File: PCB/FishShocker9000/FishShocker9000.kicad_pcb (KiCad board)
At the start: 2 copper layers, 160 parts, among them J1 Barrel_Jack, J10 P70-1000045R, J11 P70-1000045R, J12 P70-1000045R, J13 P70-1000045R, J14 P70-1000045R, J15 P70-1000045R, J16 P70-1000045R, J17 P70-1000045R, J18 P70-1000045R, J19 P70-1000045R, J20 P70-1000045R, J21 P70-1000045R, J22 P70-1000045R, J23 P70-1000045R, J24 P70-1000045R, J25 P70-1000045R, J26 P70-1000045R, J27 P70-1000045R, J28 P70-1000045R, J29 P70-1000045R, J3 P70-1000045R, J30 P70-1000045R, J31 P70-1000045R, J32 P70-1000045R, J33 P70-1000045R, J34 P70-1000045R, J35 P70-1000045R, J36 P70-1000045R, J37 P70-1000045R, J38 P70-1000045R, J39 P70-1000045R, J4 P70-1000045R, J40 P70-1000045R, J41 P70-1000045R, J42 P70-1000045R, J43 P70-1000045R, J44 P70-1000045R, J45 P70-1000045R, J46 P70-1000045R, J47 P70-1000045R, J48 P70-1000045R, J49 P70-1000045R, J5 P70-1000045R, J50 P70-1000045R, J51 P70-1000045R, J52 P70-1000045R, J53 P70-1000045R, J54 P70-1000045R, J55 P70-1000045R, J56 P70-1000045R, J57 P70-1000045R, J58 P70-1000045R, J59 P70-1000045R, J6 P70-1000045R, J60 P70-1000045R, J61 P70-1000045R, J62 P70-1000045R, J63 P70-1000045R, J64 P70-1000045R, J65 P70-1000045R, J66 P70-1000045R, J67 P70-1000045R, J68 P70-1000045R, J69 P70-1000045R, J7 P70-1000045R, J70 P70-1000045R, J71 P70-1000045R, J72 P70-1000045R, J73 P70-1000045R, J74 P70-1000045R, J75 Screw_Terminal_01x02, J8 P70-1000045R, J9 P70-1000045R, Q2 FQP27P06, U10 SN754410NE, U11 SN754410NE, U12 SN754410NE, U13 SN754410NE, U14 SN754410NE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

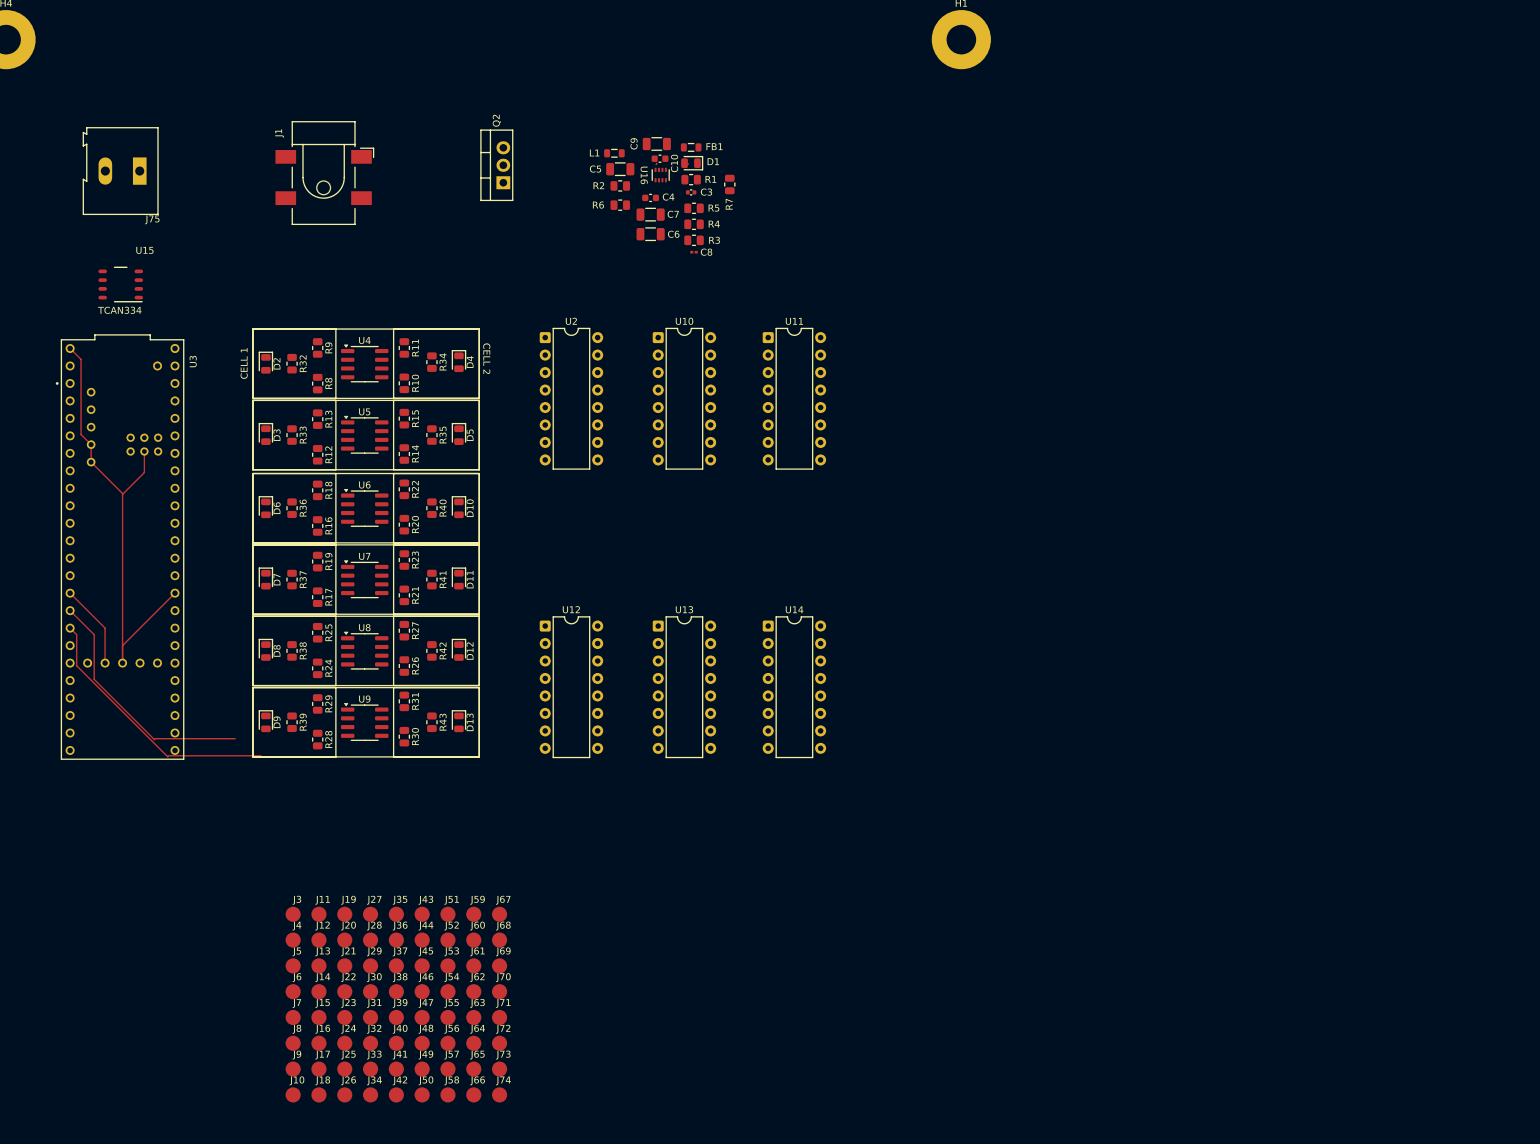
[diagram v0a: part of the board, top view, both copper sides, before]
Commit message: routed PCB except for GND and Pogo Pins
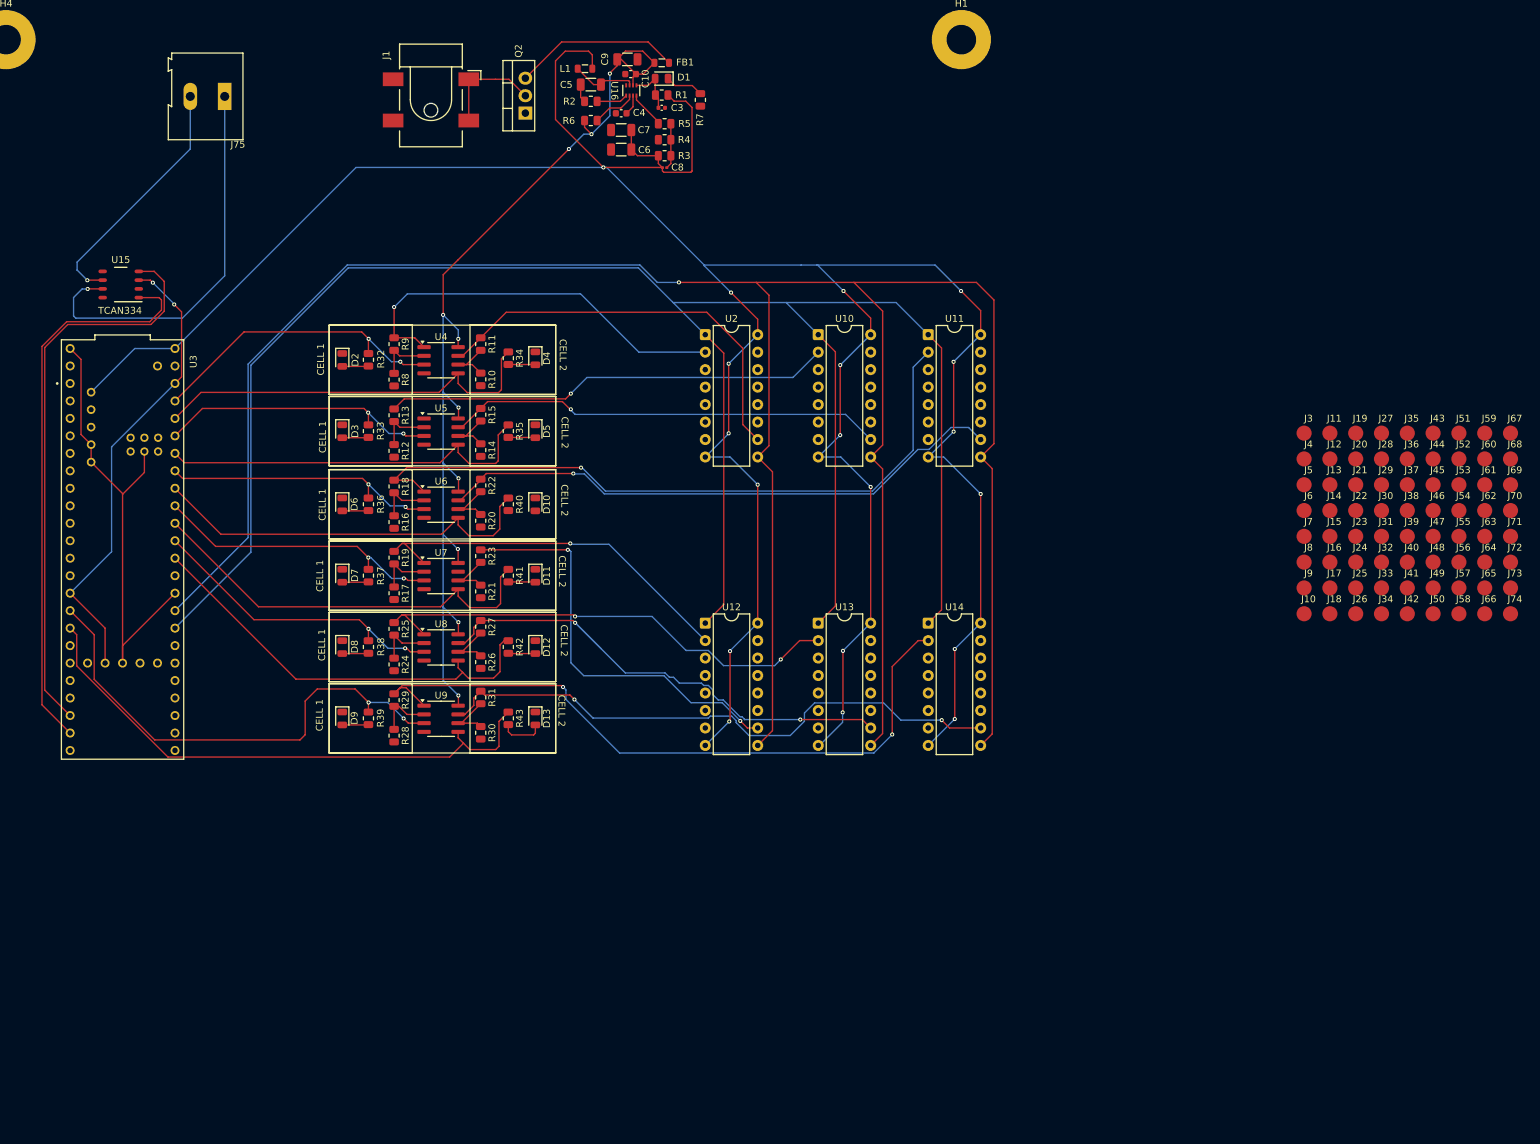
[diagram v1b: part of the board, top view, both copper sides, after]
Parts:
- moved J10 162.7 mm to (205.8, 101.5)
- moved J11 162.7 mm to (209.6, 75.3)
- moved J12 162.7 mm to (209.6, 79.0)
- moved J13 162.7 mm to (209.6, 82.8)
- moved J14 162.7 mm to (209.6, 86.5)
- moved J15 162.7 mm to (209.6, 90.3)
- moved J16 162.7 mm to (209.6, 94.0)
- moved J17 162.7 mm to (209.6, 97.8)
- moved J18 162.7 mm to (209.6, 101.5)
- moved J19 162.7 mm to (213.3, 75.3)
- moved J20 162.7 mm to (213.3, 79.0)
- moved J21 162.7 mm to (213.3, 82.8)
- moved J22 162.7 mm to (213.3, 86.5)
- moved J23 162.7 mm to (213.3, 90.3)
- moved J24 162.7 mm to (213.3, 94.0)
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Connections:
- R32 pad 1: A0 -> A9
- R33 pad 1: A2 -> A7
- R34 pad 1: A1 -> A8
- R35 pad 1: A3 -> A6
- R36 pad 1: A4 -> A5
- R37 pad 1: A6 -> A3
- R38 pad 1: A8 -> A1
- R40 pad 1: A5 -> A4
- R41 pad 1: A7 -> A2
- R42 pad 1: A9 -> A0
- U4 pad 3: A0 -> A9
- U4 pad 5: A1 -> A8
- U5 pad 3: A2 -> A7
- U5 pad 5: A3 -> A6
- U6 pad 3: A4 -> A5
- U6 pad 5: A5 -> A4
- U7 pad 3: A6 -> A3
- U7 pad 5: A7 -> A2
- U8 pad 3: A8 -> A1
- U8 pad 5: A9 -> A0
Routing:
- net BUCK_VOUT: track 0.00 -> 457.6 mm, vias 0 -> 19
- net Polarity Enable 2: track 0.00 -> 365.3 mm, vias 0 -> 1
- net Polarity Enable 1: track 0.00 -> 296.0 mm
- net AMP_RAIL: track 0.00 -> 149.4 mm, vias 0 -> 10
- net CELL11: track 0.00 -> 101.3 mm, vias 0 -> 2
- net CELL5: track 0.00 -> 100.3 mm, vias 0 -> 1
- net CELL12: track 0.00 -> 85.2 mm, vias 0 -> 2
- net CELL6: track 0.00 -> 83.6 mm, vias 0 -> 1
- net RXD: track 0.00 -> 83.2 mm
- net TXD: track 0.00 -> 82.3 mm
- net CELL10: track 0.00 -> 74.1 mm, vias 0 -> 2
- net CELL9: track 0.00 -> 71.1 mm, vias 0 -> 2
- net CELL3: track 0.00 -> 65.1 mm, vias 0 -> 1
- net CELL4: track 0.00 -> 63.8 mm, vias 0 -> 1
- net A0: track 0.00 -> 63.0 mm
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
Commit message: New draft of final PCB layout
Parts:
- added Q1: IRLZ44N, Package_TO_SOT_THT:TO-220-3_Vertical, F.Cu at (123.6, 22.4)
- R7: value 220 -> 330
- moved J10 143.6 mm to (80.2, 171.1)
- moved J11 143.6 mm to (83.9, 144.8)
- moved J12 143.6 mm to (83.9, 148.6)
- moved J13 143.6 mm to (83.9, 152.3)
- moved J14 143.6 mm to (83.9, 156.1)
- moved J15 143.6 mm to (83.9, 159.8)
- moved J16 143.6 mm to (83.9, 163.6)
- moved J17 143.6 mm to (83.9, 167.3)
- moved J18 143.6 mm to (83.9, 171.1)
- moved J19 143.6 mm to (87.7, 144.8)
- moved J20 143.6 mm to (87.7, 148.6)
- moved J21 143.6 mm to (87.7, 152.3)
- moved J22 143.6 mm to (87.7, 156.1)
- moved J23 143.6 mm to (87.7, 159.8)
- moved J24 143.6 mm to (87.7, 163.6)
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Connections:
- net AMP_RAIL renamed BUCK_IN
- D1 pad 2: BUCK_PG -> Net-(D1-A)
- R7 pad 1: GND -> Net-(D1-A)
- R7 pad 2: Net-(D1-K) -> BUCK_VOUT
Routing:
- net GND: track 69.7 -> 138.9 mm, vias 0 -> 4
- net BUCK_PG: track 7.56 -> 21.8 mm, vias 0 -> 1
- net Net-(D1-A): track 0.00 -> 7.48 mm
- net Net-(D10-A): track 0.00 -> 6.54 mm
- net Net-(D1-K): track 5.61 -> 11.7 mm
- net CELL8: track 60.5 -> 65.6 mm
- net CELL3: track 65.1 -> 69.4 mm
- net BUCK_IN: track 149.4 -> 146.0 mm
- net Net-(D12-A): track 3.95 -> 5.37 mm
- net Net-(D4-A): track 3.95 -> 5.33 mm
- net BUCK_VOUT: track 457.6 -> 458.9 mm
- net Net-(D5-A): track 3.95 -> 5.15 mm
- net Net-(D13-A): track 6.46 -> 7.19 mm
- net CELL9: vias 2 -> 1
- added copper zone on F.Cu, net GND
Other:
- board text added: "Barrel Jack"
- board text added: "CAN Bus H/L"
- board text added: "CELL 10"
- board text added: "CELL 11"
- board text added: "CELL 12"
- board text added: "CELL 3"
- board text added: "CELL 4"
- board text added: "CELL 5"
- board text added: "CELL 6"
- board text added: "CELL 7"
- board text added: "CELL 8"
- board text added: "CELL 9"
- board text added: "LED ON = GOOD POWER"
- board text added: "Op-Amps"
- board text added: "Polarity Drivers"
- board text added: "Teensy 4.1"

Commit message: Changed Layout to eb more clean
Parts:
- moved J10 141.4 mm to (194.8, 88.3)
- moved J11 141.4 mm to (198.5, 62.1)
- moved J12 141.4 mm to (198.5, 65.8)
- moved J13 141.4 mm to (198.5, 69.6)
- moved J14 141.4 mm to (198.5, 73.3)
- moved J15 141.4 mm to (198.5, 77.1)
- moved J16 141.4 mm to (198.5, 80.8)
- moved J17 141.4 mm to (198.5, 84.6)
- moved J18 141.4 mm to (198.5, 88.3)
- moved J19 141.4 mm to (202.3, 62.1)
- moved J20 141.4 mm to (202.3, 65.8)
- moved J21 141.4 mm to (202.3, 69.6)
- moved J22 141.4 mm to (202.3, 73.3)
- moved J23 141.4 mm to (202.3, 77.1)
- moved J24 141.4 mm to (202.3, 80.8)
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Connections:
- U10 pad 10: CELL4 -> CELL3
- U10 pad 11: Plate 4.1 -> Plate 3.2
- U10 pad 14: Plate 4.2 -> Plate 3.1
- U10 pad 2: CELL3 -> CELL4
- U10 pad 3: Plate 3.1 -> Plate 4.2
- U10 pad 6: Plate 3.2 -> Plate 4.1
- U11 pad 10: CELL6 -> CELL5
- U11 pad 11: Plate 6.1 -> Plate 5.2
- U11 pad 14: Plate 6.2 -> Plate 5.1
- U11 pad 2: CELL5 -> CELL6
- U11 pad 3: Plate 5.1 -> Plate 6.2
- U11 pad 6: Plate 5.2 -> Plate 6.1
- U12 pad 10: CELL8 -> CELL7
- U12 pad 11: Plate 8.1 -> Plate 7.2
- U12 pad 14: Plate 8.2 -> Plate 7.1
- U12 pad 2: CELL7 -> CELL8
- U12 pad 3: Plate 7.1 -> Plate 8.2
- U12 pad 6: Plate 7.2 -> Plate 8.1
- U13 pad 10: CELL10 -> CELL9
- U13 pad 11: Plate 10.1 -> Plate 9.2
- U13 pad 14: Plate 10.2 -> Plate 9.1
- U13 pad 2: CELL9 -> CELL10
- U13 pad 3: Plate 9.1 -> Plate 10.2
- U13 pad 6: Plate 9.2 -> Plate 10.1
- U14 pad 10: CELL12 -> CELL11
- U14 pad 11: Plate 12.1 -> Plate 11.2
- U14 pad 14: Plate 12.2 -> Plate 11.1
- U14 pad 2: CELL11 -> CELL12
- U14 pad 3: Plate 11.1 -> Plate 12.2
- U14 pad 6: Plate 11.2 -> Plate 12.1
- U2 pad 10: CELL2 -> CELL1
- U2 pad 11: Plate 2.1 -> Plate 1.2
- U2 pad 14: Plate 2.2 -> Plate 1.1
- U2 pad 2: CELL1 -> CELL2
- U2 pad 3: Plate 1.1 -> Plate 2.2
- U2 pad 6: Plate 1.2 -> Plate 2.1
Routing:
- net BUCK_IN: track 146.0 -> 216.6 mm, vias 10 -> 7
- net Polarity Enable 2: track 365.3 -> 299.4 mm, vias 1 -> 0
- net CELL12: track 85.2 -> 53.5 mm, vias 2 -> 0
- net CELL6: track 83.6 -> 53.3 mm, vias 1 -> 0
- net BUCK_VOUT: track 458.9 -> 429.8 mm, vias 19 -> 1
- net Polarity Enable 1: track 296.0 -> 269.3 mm
- net CELL11: track 101.3 -> 77.1 mm, vias 2 -> 0
- net A9: track 44.5 -> 68.1 mm
- net CELL5: track 100.3 -> 77.6 mm, vias 1 -> 0
- net CELL7: track 55.9 -> 77.3 mm, vias 1 -> 0
- net CELL10: track 74.1 -> 54.0 mm, vias 2 -> 0
- net BARREL_21V: track 15.2 -> 34.7 mm
- net CELL1: track 58.9 -> 78.3 mm, vias 1 -> 0
- net Plate 1.1: track 0.00 -> 17.9 mm
- net A11: track 81.7 -> 98.5 mm
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
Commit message: added various items to the schematic
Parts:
- removed J75: Screw_Terminal_01x02, TerminalBlock:TerminalBlock_Altech_AK300-2_P5.00mm
- removed R20, R21, R24, R26, R28, R30: 3.3k, Resistor_SMD:R_0805_2012Metric
- removed R22, R23, R25, R27, R29, R31: 15k, Resistor_SMD:R_0805_2012Metric
- removed R32, R33, R34, R35, R36, R37, R38, R39, R40, R41, R42, R43: 220, Resistor_SMD:R_0805_2012Metric
- removed U10, U11, U12, U13, U14, U2: SN754410NE, Package_DIP:DIP-16_W7.62mm
- removed U15: TCAN334, Library:D0008A_L
- removed U4, U5, U6, U7, U8, U9: OPA2197xD, Package_SO:SOIC-8_3.9x4.9mm_P1.27mm
- added R48: 4.7k, Resistor_THT:R_Bare_Metal_Element_L12.4mm_W4.8mm_P11.40mm, F.Cu at (46.5, 28.5)
- added R49: 15k, Resistor_THT:R_Bare_Metal_Element_L12.4mm_W4.8mm_P11.40mm, F.Cu at (57.0, 28.5)
- added U19: DAC5311xDCK, Package_TO_SOT_SMD:SOT-363_SC-70-6, F.Cu at (36.3, 28.3)
- added U20: OPA197xD, Package_SO:SOIC-8_3.9x4.9mm_P1.27mm, F.Cu at (36.5, 19.3)
- added U23: SN754410NE, Package_DIP:DIP-16_W7.62mm, F.Cu at (106.4, 104.0)
- added U24: SN754410NE, Package_DIP:DIP-16_W7.62mm, F.Cu at (106.4, 93.2)
- added U25: SN754410NE, Package_DIP:DIP-16_W7.62mm, F.Cu at (106.4, 82.4)
- added U26: SN754410NE, Package_DIP:DIP-16_W7.62mm, F.Cu at (106.4, 71.6)
- added U29: SN754410NE, Package_DIP:DIP-16_W7.62mm, F.Cu at (106.4, 60.8)
- added U30: SN754410NE, Package_DIP:DIP-16_W7.62mm, F.Cu at (106.4, 50.1)
- D10, D11, D12, D13, D2, D3, D4, D5, D6, D7, D8, D9: value GREEN -> LED
- R10, R12, R14, R16, R17, R8: value 3.3k -> 220
- R11, R13, R15, R18, R19, R9: value 15k -> 220
- moved D13 100.6 mm to (63.5, 67.6), turned to 0 degrees
- moved D9 95.0 mm to (59.1, 67.6), turned to 0 degrees
- moved D12 84.0 mm to (63.5, 64.5), turned to 0 degrees
- moved D8 77.3 mm to (59.1, 64.5), turned to 0 degrees
- moved D11 67.8 mm to (63.5, 61.5), turned to 0 degrees
- moved D7 59.1 mm to (59.1, 61.5), turned to 0 degrees
- moved D10 53.0 mm to (63.5, 58.5), turned to 0 degrees
- moved R17 50.7 mm to (63.4, 73.5), turned to 0 degrees
- moved D5 44.8 mm to (54.6, 67.6), turned to 0 degrees
- moved D4 44.7 mm to (54.6, 64.5), turned to 0 degrees
- moved R11 43.9 mm to (54.6, 79.4), turned to 0 degrees
- moved D6 41.5 mm to (59.1, 58.5), turned to 0 degrees
- moved U3 40.6 mm to (37.5, 71.5)
- moved R19 40.2 mm to (63.4, 79.4), turned to 0 degrees
- moved R10 39.9 mm to (54.6, 76.5), turned to 0 degrees
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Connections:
- R10 pad 1: Net-(U4B--) -> A4
- R10 pad 2: GND -> Net-(D4-A)
- R11 pad 1: CELL2 -> A5
- R11 pad 2: Net-(U4B--) -> Net-(D5-A)
- R12 pad 1: Net-(U5A--) -> A8
- R12 pad 2: GND -> Net-(D6-A)
- R13 pad 1: CELL3 -> A9
- R13 pad 2: Net-(U5A--) -> Net-(D7-A)
- R14 pad 1: Net-(U5B--) -> A2
- R14 pad 2: GND -> Net-(D8-A)
- R15 pad 1: CELL4 -> A6
- R15 pad 2: Net-(U5B--) -> Net-(D9-A)
- R16 pad 1: Net-(U6A--) -> A10
- R16 pad 2: GND -> Net-(D10-A)
- R17 pad 1: Net-(U7A--) -> A3
- R17 pad 2: GND -> Net-(D11-A)
- R18 pad 1: CELL5 -> A7
- R18 pad 2: Net-(U6A--) -> Net-(D12-A)
- R19 pad 1: CELL7 -> A11
- R19 pad 2: Net-(U7A--) -> Net-(D13-A)
- R8 pad 1: Net-(U4A--) -> A0
- R8 pad 2: GND -> Net-(D2-A)
- R9 pad 1: CELL1 -> A1
- R9 pad 2: Net-(U4A--) -> Net-(D3-A)
- U3 pad 11: unconnected-(U3-MOSI-Pad11) -> MOSI
- U3 pad 13: unconnected-(U3-SCK-Pad13) -> SCK
- U3 pad 26: unconnected-(U3-A12-Pad26) -> SYNC
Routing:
- net BUCK_VOUT: track 429.8 -> 53.4 mm
- net Polarity Enable 2: track 299.4 -> 0.00 mm
- net Polarity Enable 1: track 269.3 -> 0.00 mm
- net BUCK_IN: track 216.6 -> 37.5 mm, vias 7 -> 0
- net GND: track 138.9 -> 39.1 mm
- net A11: track 98.5 -> 0.00 mm
- net RXD: track 83.2 -> 0.00 mm
- net TXD: track 82.3 -> 0.00 mm
- net A10: track 79.6 -> 0.00 mm, vias 2 -> 0
- net A0: track 78.8 -> 0.00 mm
- net CELL1: track 78.3 -> 0.00 mm
- net CELL5: track 77.6 -> 0.00 mm
- net CELL3: track 77.6 -> 0.00 mm
- net CELL9: track 77.5 -> 0.00 mm
- net CELL7: track 77.3 -> 0.00 mm
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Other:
- board text removed: "CAN Bus H/L"
- board text removed: "CELL 1"
- board text removed: "CELL 10"
- board text removed: "CELL 11"
- board text removed: "CELL 12"
- board text removed: "CELL 2"
- board text removed: "CELL 3"
- board text removed: "CELL 4"
- board text removed: "CELL 5"
- board text removed: "CELL 6"
- board text removed: "CELL 7"
- board text removed: "CELL 8"
- board text removed: "CELL 9"
- board text removed: "Op-Amps"
- board text removed: "Polarity Drivers"

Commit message: Made Changes but not complete PCB. Gonna reformat
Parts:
- H1, H2, H3, H4: footprint MountingHole:MountingHole_4.3mm_M4_Pad -> MountingHole:MountingHole_2.2mm_M2_DIN965_Pad
- R48, R49: footprint Resistor_THT:R_Bare_Metal_Element_L12.4mm_W4.8mm_P11.40mm -> Resistor_THT:R_Axial_DIN0207_L6.3mm_D2.5mm_P10.16mm_Horizontal
- moved D3 354.7 mm to (397.1, 154.0), turned to 180 degrees
- moved D8 346.7 mm to (397.0, 142.0), turned to 180 degrees
- moved R9 345.9 mm to (391.0, 154.0), turned to -90 degrees
- moved D6 342.9 mm to (397.1, 116.5), turned to 180 degrees
- moved D12 339.8 mm to (397.0, 129.5), turned to 180 degrees
- moved R14 338.4 mm to (391.0, 142.0), turned to -90 degrees
- moved D2 337.6 mm to (378.5, 153.8), turned to 180 degrees
- moved R12 335.2 mm to (391.0, 116.5), turned to -90 degrees
- moved D5 332.3 mm to (378.5, 142.0), turned to 180 degrees
- moved R18 331.9 mm to (391.0, 129.5), turned to -90 degrees
- moved R8 329.2 mm to (373.0, 154.0), turned to -90 degrees
- moved D9 325.4 mm to (378.5, 129.5), turned to 180 degrees
- moved R11 324.5 mm to (373.0, 142.0), turned to -90 degrees
- moved D13 318.8 mm to (378.6, 116.5), turned to 180 degrees
- moved R15 318.0 mm to (373.0, 129.5), turned to -90 degrees
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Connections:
- R10 pad 1: A4 -> A5
- R11 pad 1: A5 -> A4
- R12 pad 1: A8 -> A9
- R13 pad 1: A9 -> A8
- R14 pad 1: A2 -> A3
- R15 pad 1: A6 -> A7
- R17 pad 1: A3 -> A2
- R18 pad 1: A7 -> A6
- R8 pad 1: A0 -> A1
- R9 pad 1: A1 -> A0
- U23 pad 1: A0 -> A1
- U23 pad 9: A1 -> A0
- U24 pad 1: A2 -> A3
- U24 pad 9: A3 -> A2
- U25 pad 1: A4 -> A5
- U25 pad 9: A5 -> A4
- U26 pad 1: A6 -> A7
- U26 pad 9: A7 -> A6
- U29 pad 1: A8 -> A9
- U29 pad 9: A9 -> A8
- U3 pad 3.3V_1: 3.3v -> unconnected-(U3-3.3V-Pad3.3V_1)_1
- U3 pad 3.3V_2: 3.3v -> unconnected-(U3-3.3V-Pad3.3V_1)
- U3 pad 3.3V_3: 3.3v -> unconnected-(U3-3.3V-Pad3.3V_1)_2
- U3 pad 30: RXD -> unconnected-(U3-CRX3-Pad30)
- U3 pad 31: TXD -> unconnected-(U3-CTX3-Pad31)
- U30 pad 11: Plate 11.1 -> Plate 12.2
- U30 pad 14: Plate 11.2 -> Plate 12.1
- U30 pad 3: Plate 12.1 -> Plate 11.2
- U30 pad 6: Plate 12.2 -> Plate 11.1
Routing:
- net Polarity Enable 2: track 0.00 -> 214.9 mm
- net BUCK_IN: track 37.5 -> 252.1 mm, vias 0 -> 2
- net Polarity Enable 1: track 0.00 -> 210.3 mm
- net A11: track 0.00 -> 152.2 mm
- net A0: track 0.00 -> 138.6 mm
- net A10: track 0.00 -> 130.4 mm
- net A3: track 0.00 -> 121.5 mm
- net A6: track 0.00 -> 114.5 mm
- net A9: track 0.00 -> 113.7 mm
- net A1: track 0.00 -> 112.4 mm
- net CELL_VOLTAGE: track 0.00 -> 103.1 mm
- net A4: track 0.00 -> 102.9 mm
- net A7: track 0.00 -> 97.7 mm
- net Plate 11.1: track 0.00 -> 93.8 mm
- net Plate 11.2: track 0.00 -> 86.9 mm
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- added copper zone on F.Cu, net BUCK_VOUT
- removed copper zone on F.Cu, net GND
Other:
- board text added: "Cell 1"
- board text added: "Cell 10"
- board text added: "Cell 11"
- board text added: "Cell 12"
- board text added: "Cell 2"
- board text added: "Cell 3"
- board text added: "Cell 4"
- board text added: "Cell 5"
- board text added: "Cell 6"
- board text added: "Cell 7"
- board text added: "Cell 8"
- board text added: "Cell 9"
